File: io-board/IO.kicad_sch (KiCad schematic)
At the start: 3 parts

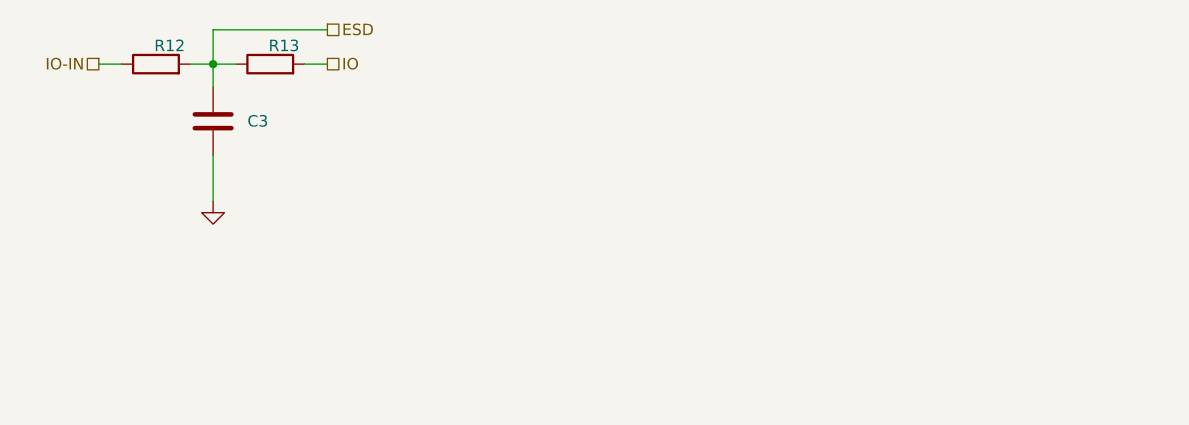
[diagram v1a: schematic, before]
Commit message: All added and connected in PCB. Cleanup needed.
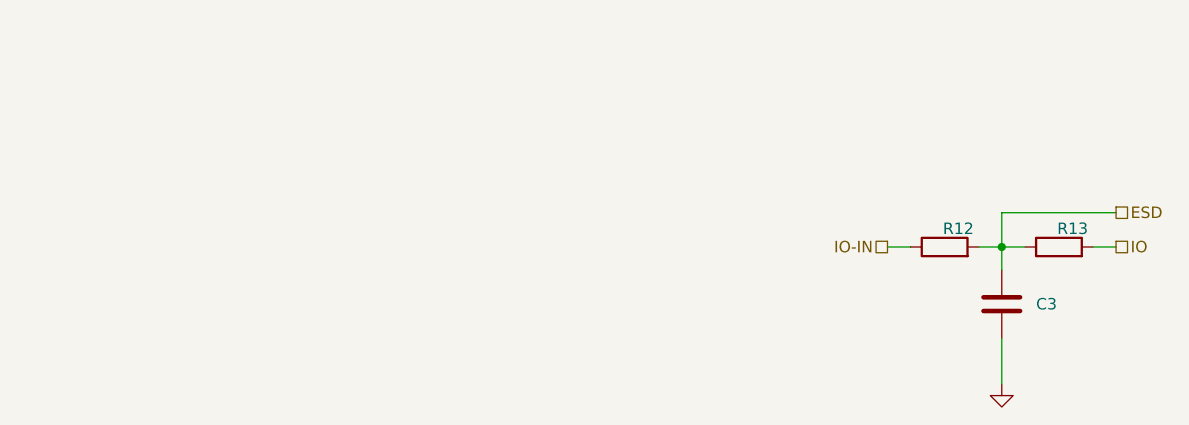
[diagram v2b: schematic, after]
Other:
- moved on the sheet: C3, R12, R13
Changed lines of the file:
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@@
 	(paper "A4")
 	(junction
-		(at 53.34 72.39)
+		(at 140.97 92.71)
 		(diameter 0)
 		(color 0 0 0 0)
@@
 	(wire
 		(pts
-			(xy 53.34 68.58) (xy 66.04 68.58)
-		)
-		(stroke
-			(width 0)
-			(type default)
-		)
-	)
-	(wire
-		(pts
-			(xy 53.34 68.58) (xy 53.34 72.39)
-		)
-		(stroke
-			(width 0)
-			(type default)
-		)
-	)
-	(wire
-		(pts
-			(xy 53.34 82.55) (xy 53.34 87.63)
-		)
-		(stroke
-			(width 0)
-			(type default)
-		)
-	)
-	(wire
-		(pts
-			(xy 53.34 72.39) (xy 53.34 74.93)
-		)
-		(stroke
-			(width 0)
-			(type default)
-		)
-	)
-	(wire
-		(pts
-			(xy 53.34 72.39) (xy 55.88 72.39)
-		)
-		(stroke
-			(width 0)
-			(type default)
-		)
-	)
-	(wire
-		(pts
-			(xy 40.64 72.39) (xy 43.18 72.39)
-		)
-		(stroke
-			(width 0)
-			(type default)
-		)
-	)
-	(wire
-		(pts
-			(xy 63.5 72.39) (xy 66.04 72.39)
-		)
-		(stroke
-			(width 0)
-			(type default)
-		)
-	)
-	(wire
-		(pts
-			(xy 50.8 72.39) (xy 53.34 72.39)
+			(xy 140.97 88.9) (xy 153.67 88.9)
+		)
+		(stroke
+			(width 0)
+			(type default)
+		)
+	)
+	(wire
+		(pts
+			(xy 140.97 88.9) (xy 140.97 92.71)
+		)
+		(stroke
+			(width 0)
+			(type default)
+		)
+	)
+	(wire
+		(pts
+			(xy 140.97 102.87) (xy 140.97 107.95)
+		)
+		(stroke
+			(width 0)
+			(type default)
+		)
+	)
+	(wire
+		(pts
+			(xy 140.97 92.71) (xy 140.97 95.25)
+		)
+		(stroke
+			(width 0)
+			(type default)
+		)
+	)
+	(wire
+		(pts
+			(xy 140.97 92.71) (xy 143.51 92.71)
+		)
+		(stroke
+			(width 0)
+			(type default)
+		)
+	)
+	(wire
+		(pts
+			(xy 128.27 92.71) (xy 130.81 92.71)
+		)
+		(stroke
+			(width 0)
+			(type default)
+		)
+	)
+	(wire
+		(pts
+			(xy 151.13 92.71) (xy 153.67 92.71)
+		)
+		(stroke
+			(width 0)
+			(type default)
+		)
+	)
+	(wire
+		(pts
+			(xy 138.43 92.71) (xy 140.97 92.71)
 		)
 		(stroke
@@
 	(hierarchical_label "ESD"
 		(shape passive)
-		(at 66.04 68.58 0)
+		(at 153.67 88.9 0)
 		(effects
 			(font
@@
 	(hierarchical_label "IO-IN"
 		(shape passive)
-		(at 40.64 72.39 180)
+		(at 128.27 92.71 180)
 		(effects
 			(font
@@
 	(hierarchical_label "IO"
 		(shape passive)
-		(at 66.04 72.39 0)
+		(at 153.67 92.71 0)
 		(effects
 			(font
@@
 	(symbol
 		(lib_id "power:GND")
-		(at 53.34 87.63 0)
+		(at 140.97 107.95 0)
 		(unit 1)
 		(exclude_from_sim no)
@@
 		(fields_autoplaced yes)
 		(property "Reference" "#PWR023"
-			(at 53.34 93.98 0)
+			(at 140.97 114.3 0)
 			(effects
 				(font
@@
 		)
 		(property "Value" "GND"
-			(at 53.34 92.71 0)
+			(at 140.97 113.03 0)
 			(effects
 				(font
@@
 		)
 		(property "Footprint" ""
-			(at 53.34 87.63 0)
+			(at 140.97 107.95 0)
 			(effects
 				(font
@@
 		)
 		(property "Datasheet" ""
-			(at 53.34 87.63 0)
+			(at 140.97 107.95 0)
 			(effects
 				(font
@@
 		)
 		(property "Description" "Power symbol creates a global label with name \"GND\" , ground"
-			(at 53.34 87.63 0)
+			(at 140.97 107.95 0)
 			(effects
 				(font
@@
 	(symbol
 		(lib_id "Device:R")
-		(at 59.69 72.39 90)
+		(at 147.32 92.71 90)
 		(unit 1)
 		(exclude_from_sim no)
@@
 		(dnp no)
 		(property "Reference" "R13"
-			(at 61.214 70.358 90)
+			(at 148.844 90.678 90)
 			(effects
 				(font
@@
 		)
 		(property "Value" "R"
-			(at 57.912 70.358 90)
+			(at 145.542 90.678 90)
 			(effects
 				(font
@@
 		)
 		(property "Footprint" "Resistor_SMD:R_0805_2012Metric_Pad1.20x1.40mm_HandSolder"
-			(at 59.69 74.168 90)
+			(at 147.32 94.488 90)
 			(effects
 				(font
@@
 		)
 		(property "Datasheet" "~"
-			(at 59.69 72.39 0)
+			(at 147.32 92.71 0)
 			(effects
 				(font
@@
 		)
 		(property "Description" "Resistor"
-			(at 59.69 72.39 0)
+			(at 147.32 92.71 0)
 			(effects
 				(font
@@
 	(symbol
 		(lib_id "Device:R")
-		(at 46.99 72.39 90)
+		(at 134.62 92.71 90)
 		(unit 1)
 		(exclude_from_sim no)
@@
 		(dnp no)
 		(property "Reference" "R12"
-			(at 48.514 70.358 90)
+			(at 136.144 90.678 90)
 			(effects
 				(font
@@
 		)
 		(property "Value" "R"
-			(at 45.212 70.358 90)
+			(at 132.842 90.678 90)
 			(effects
 				(font
@@
 		)
 		(property "Footprint" "Resistor_SMD:R_0805_2012Metric_Pad1.20x1.40mm_HandSolder"
-			(at 46.99 74.168 90)
+			(at 134.62 94.488 90)
 			(effects
 				(font
@@
 		)
 		(property "Datasheet" "~"
-			(at 46.99 72.39 0)
+			(at 134.62 92.71 0)
 			(effects
 				(font
@@
 		)
 		(property "Description" "Resistor"
-			(at 46.99 72.39 0)
+			(at 134.62 92.71 0)
 			(effects
 				(font
@@
 	(symbol
 		(lib_id "Device:C")
-		(at 53.34 78.74 0)
+		(at 140.97 99.06 0)
 		(unit 1)
 		(exclude_from_sim no)
@@
 		(fields_autoplaced yes)
 		(property "Reference" "C3"
-			(at 57.15 78.7399 0)
+			(at 144.78 99.0599 0)
 			(effects
 				(font
@@
 		)
 		(property "Value" "C"
-			(at 57.15 80.0099 0)
+			(at 144.78 100.3299 0)
 			(effects
 				(font
@@
 		)
 		(property "Footprint" "Capacitor_SMD:C_0805_2012Metric_Pad1.18x1.45mm_HandSolder"
-			(at 54.3052 82.55 0)
+			(at 141.9352 102.87 0)
 			(effects
 				(font
@@
 		)
 		(property "Datasheet" "~"
-			(at 53.34 78.74 0)
+			(at 140.97 99.06 0)
 			(effects
 				(font
@@
 		)
 		(property "Description" "Unpolarized capacitor"
-			(at 53.34 78.74 0)
-			(effects
-				(font
+			(at 140.97 99.06 0)
+			(effects
+				(font

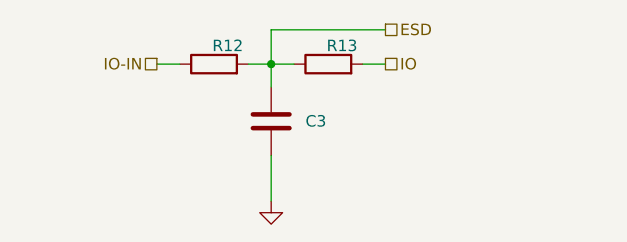
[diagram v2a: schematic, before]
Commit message: PCB: io-board: component values and BOM
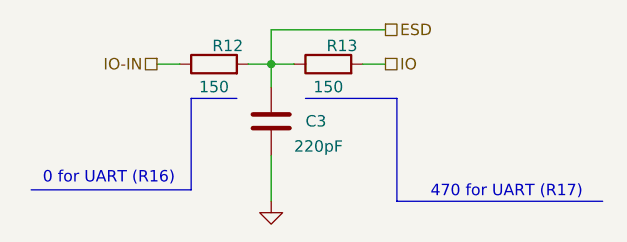
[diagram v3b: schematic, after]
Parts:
- C3: value C -> 220pF
- R12, R13: value R -> 150
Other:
- note added: "0 for UART (R16)"
- note added: "470 for UART (R17)"
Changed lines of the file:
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@@
 	(generator_version "9.0")
 	(paper "A4")
+	(text "0 for UART (R16)"
+		(exclude_from_sim no)
+		(at 122.936 105.41 0)
+		(effects
+			(font
+				(size 1.27 1.27)
+			)
+		)
+	)
+	(text "470 for UART (R17)"
+		(exclude_from_sim no)
+		(at 167.132 106.934 0)
+		(effects
+			(font
+				(size 1.27 1.27)
+			)
+		)
+	)
 	(junction
 		(at 140.97 92.71)
@@
 		(color 0 0 0 0)
 	)
+	(polyline
+		(pts
+			(xy 154.94 96.52) (xy 154.94 107.95)
+		)
+		(stroke
+			(width 0)
+			(type default)
+		)
+	)
+	(polyline
+		(pts
+			(xy 144.78 96.52) (xy 154.94 96.52)
+		)
+		(stroke
+			(width 0)
+			(type default)
+		)
+	)
 	(wire
 		(pts
@@
 		)
 	)
+	(polyline
+		(pts
+			(xy 154.94 107.95) (xy 177.8 107.95)
+		)
+		(stroke
+			(width 0)
+			(type default)
+		)
+	)
 	(wire
 		(pts
@@
 		)
 	)
+	(polyline
+		(pts
+			(xy 132.08 106.68) (xy 132.08 96.52)
+		)
+		(stroke
+			(width 0)
+			(type default)
+		)
+	)
+	(polyline
+		(pts
+			(xy 132.08 96.52) (xy 137.16 96.52)
+		)
+		(stroke
+			(width 0)
+			(type default)
+		)
+	)
 	(wire
 		(pts
 			(xy 138.43 92.71) (xy 140.97 92.71)
+		)
+		(stroke
+			(width 0)
+			(type default)
+		)
+	)
+	(polyline
+		(pts
+			(xy 114.3 106.68) (xy 132.08 106.68)
 		)
 		(stroke
@@
 			)
 		)
-		(property "Value" "R"
-			(at 145.542 90.678 90)
-			(effects
-				(font
-					(size 1.27 1.27)
-				)
-				(hide yes)
+		(property "Value" "150"
+			(at 147.32 95.25 90)
+			(effects
+				(font
+					(size 1.27 1.27)
+				)
 			)
 		)
@@
 			)
 		)
-		(property "Value" "R"
-			(at 132.842 90.678 90)
-			(effects
-				(font
-					(size 1.27 1.27)
-				)
-				(hide yes)
+		(property "Value" "150"
+			(at 134.62 95.25 90)
+			(effects
+				(font
+					(size 1.27 1.27)
+				)
 			)
 		)
@@
 		(on_board yes)
 		(dnp no)
-		(fields_autoplaced yes)
 		(property "Reference" "C3"
 			(at 144.78 99.0599 0)
@@
 			)
 		)
-		(property "Value" "C"
-			(at 144.78 100.3299 0)
+		(property "Value" "220pF"
+			(at 143.51 101.854 0)
 			(effects
 				(font
@@
 				)
 				(justify left)
-				(hide yes)
-			)
-		)
+			)
+		)

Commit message: New CAN-based physical layer, application protocol description, hi-res timers drafts.
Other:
- note added: "20p for UART (C1)"
- note removed: "470 for UART (R17)"
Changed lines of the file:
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@@
 		)
 	)
-	(text "470 for UART (R17)"
+	(text "20p for UART (C1)"
 		(exclude_from_sim no)
-		(at 167.132 106.934 0)
+		(at 165.862 113.284 0)
 		(effects
 			(font
 				(size 1.27 1.27)
 			)
+		)
+	)
+	(text_box "https://www.falstad.com/circuit/circuitjs.html?ctz=CQAgjOCmC0AcIFYB0BOAzAFgEwoQBjQDYB2NFLPeBKxPRGMMAKACcQMxCQsM6NY6WYlhB9ieCUwBK7Tt16yuYcqNUK0SNKrp4kCJgGN2A7sMUg0eDO24MIuifaSPRSZmwyFrXiwhE+6MHxpEGh+cCx4MPgsHlURBGJCCXA9VIRtPSYAc3NLaw4uNCJtJgB3dh8fBGSQAPK6uKq4oRE8BsIWs06C+tzC9hQuAb94HUNjPh8BjCGbLDtXFwc8J2YZGbQRAbRYax12Og0tA919DzkMLcnK-fZxSQuuHpvCGrUH9o25F5Gk7UOFk0ALOE34dDewx+sHg1gW0EYS1WSLWOXMhBh5mEpw6cU83ia73aTxAsEuJj2Y3uEi+5jJUK4SSpfCOwNOWSM4NJ4QGML4tgRTmWzmRumY-TkfPMKDAbVEuO87xelPlJLAElhJnVCjENJCA3VlGltQO6jZmX0nK1Vj4cnVZjhixWQtFblYN21ELintUQXaEqUeAddu1pQqyvCLx97SMaD8dWscZEYAwBQFiOdKPluST4FTvmTKnGvC0xD2pMCsCaRqOAH0MLW8LXZQgMAhGyLVh2aWBawja1ha2ghw1WtyYmZo6OzCqx5D5RU5+8x-j5QBlcC1MfXMeBEAAMwAhgAbADOkHiaJ3mOuxS44xkO-e1zA-1NrJOFqYp9M2x8Y93VQjzPSBv03QQzAAsw92A88mH3UJ8lCCgokYERoBQiw2iQT4aTwvChSwNEU2sEi8zhGsF3I8BZWo+o2FzI54wCalJEfeMmPQ8J3yBT8dCyAAHEBSC4OA6BE4wLABQ18I6TExOEkoFP9RThngCS0LDRpvAJaxlLkqITBefSZBqOhoGqWpoDmHjjhBLI2DM0JLPMuRAjwhonIRLgnPqAAXCsIngMjZSpexfRSAATSAjwAV2PPz3S1SJQnCUL4goBplHQzDdj02J9k82pmh01Vf3AG0PUqwJgjYMcVS5FUauJG4VQjMLavK+cuXnZr3R6pVCXvcBOpXaYTFXPqPAmkrbl9TqyJ8XMWL9fqTDnLo5VWurIIddboJG9oAHtuE3KTeBQGgHAyOgMkTU7BHOm6mCAA"
+		(exclude_from_sim no)
+		(at 12.7 193.04 0)
+		(size 147.32 3.81)
+		(margins 0.9525 0.9525 0.9525 0.9525)
+		(stroke
+			(width 0)
+			(type solid)
+		)
+		(fill
+			(type none)
+		)
+		(effects
+			(font
+				(size 1.27 1.27)
+			)
+			(justify left top)
+		)
+	)
+	(text_box "For UART:"
+		(exclude_from_sim no)
+		(at 12.7 186.69 0)
+		(size 85.09 5.08)
+		(margins 0.9525 0.9525 0.9525 0.9525)
+		(stroke
+			(width 0)
+			(type solid)
+		)
+		(fill
+			(type none)
+		)
+		(effects
+			(font
+				(size 1.27 1.27)
+			)
+			(justify left top)
 		)
 	)
@@
 	(polyline
 		(pts
-			(xy 154.94 96.52) (xy 154.94 107.95)
+			(xy 153.67 102.87) (xy 153.67 114.3)
 		)
 		(stroke
@@
 	(polyline
 		(pts
-			(xy 144.78 96.52) (xy 154.94 96.52)
+			(xy 143.51 102.87) (xy 153.67 102.87)
 		)
 		(stroke
@@
 	(polyline
 		(pts
-			(xy 154.94 107.95) (xy 177.8 107.95)
+			(xy 153.67 114.3) (xy 176.53 114.3)
 		)
 		(stroke
